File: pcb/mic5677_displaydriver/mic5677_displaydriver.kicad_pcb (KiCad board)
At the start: 2 copper layers, 180 x 110 mm, 81 parts, among them J1 Segment DIP14, J2 Segment DIP14, J3 Segment Wire Connector, J4 Common Cathode Enable, J5 PSU, J6 Bypass, J7 Serial Debug, J8 8P8C, Q1 D45H8G, Q10 BC546, Q11 BC546, Q12 BC546, Q13 BC546, Q14 BC546, Q15 BC546, Q16 BC546, Q17 BC546, Q18 BC546, Q19 BC546, Q2 D45H8G, Q20 BC546, Q21 BC546, Q22 BC546, Q23 BC546, Q3 D45H8G, Q4 D45H8G, Q5 D45H8G, Q6 D45H8G, Q7 D45H8G, Q8 D45H8G, Q9 D45H8G, U1 L7805, U2 74HC595, U3 74HC595, U4 74HC02

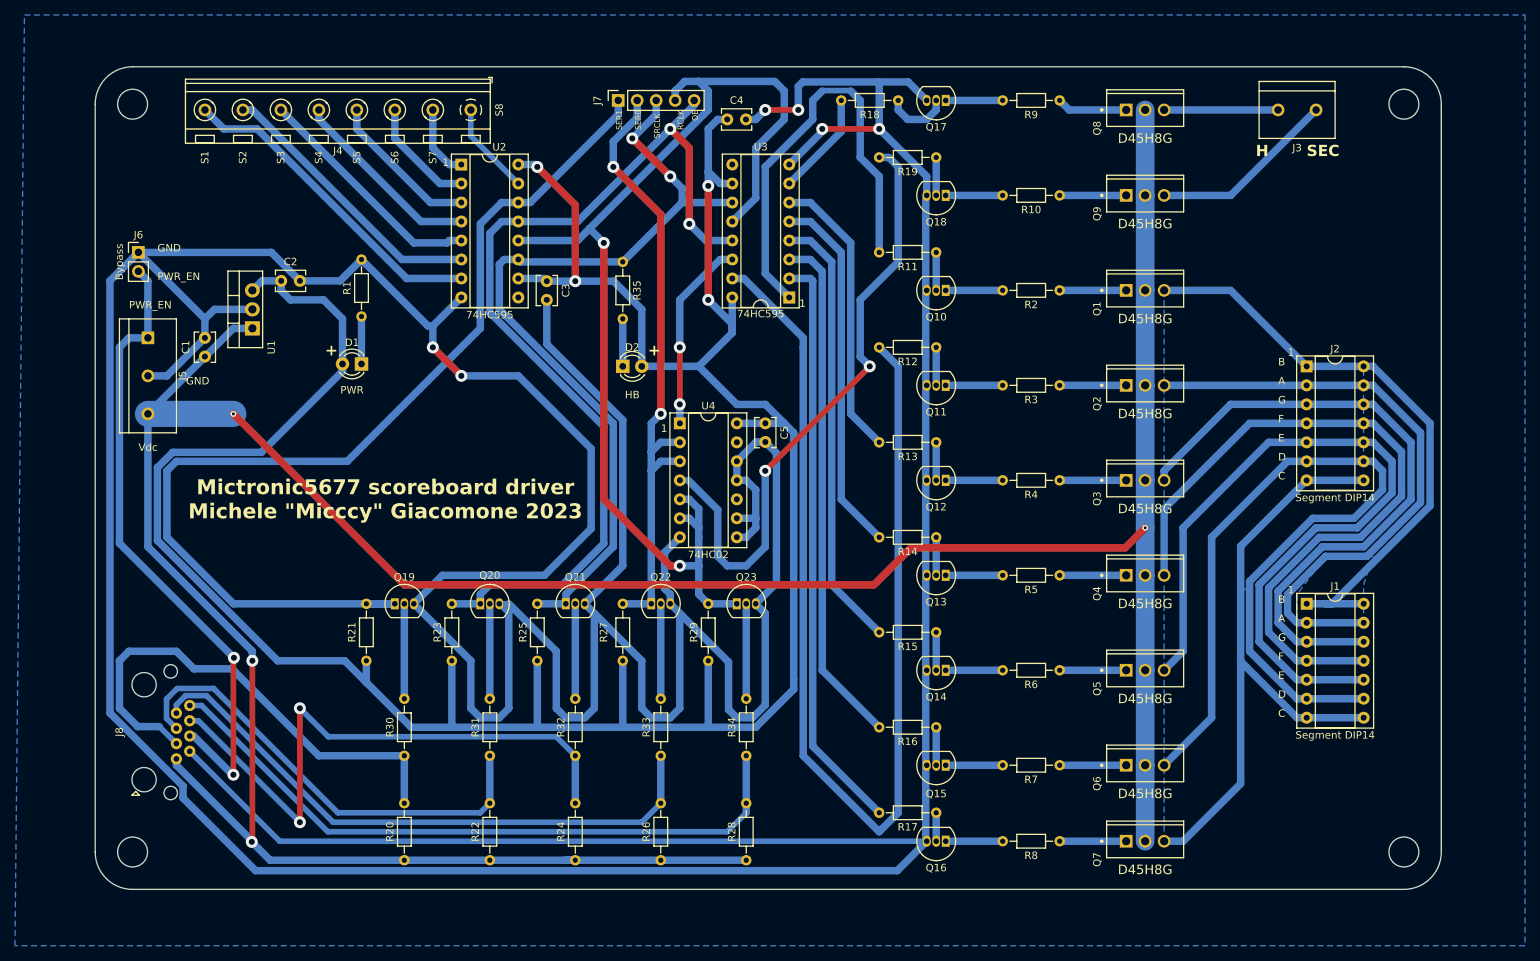
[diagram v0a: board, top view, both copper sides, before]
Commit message: Made display driver pcb work both with and without filled fill zones
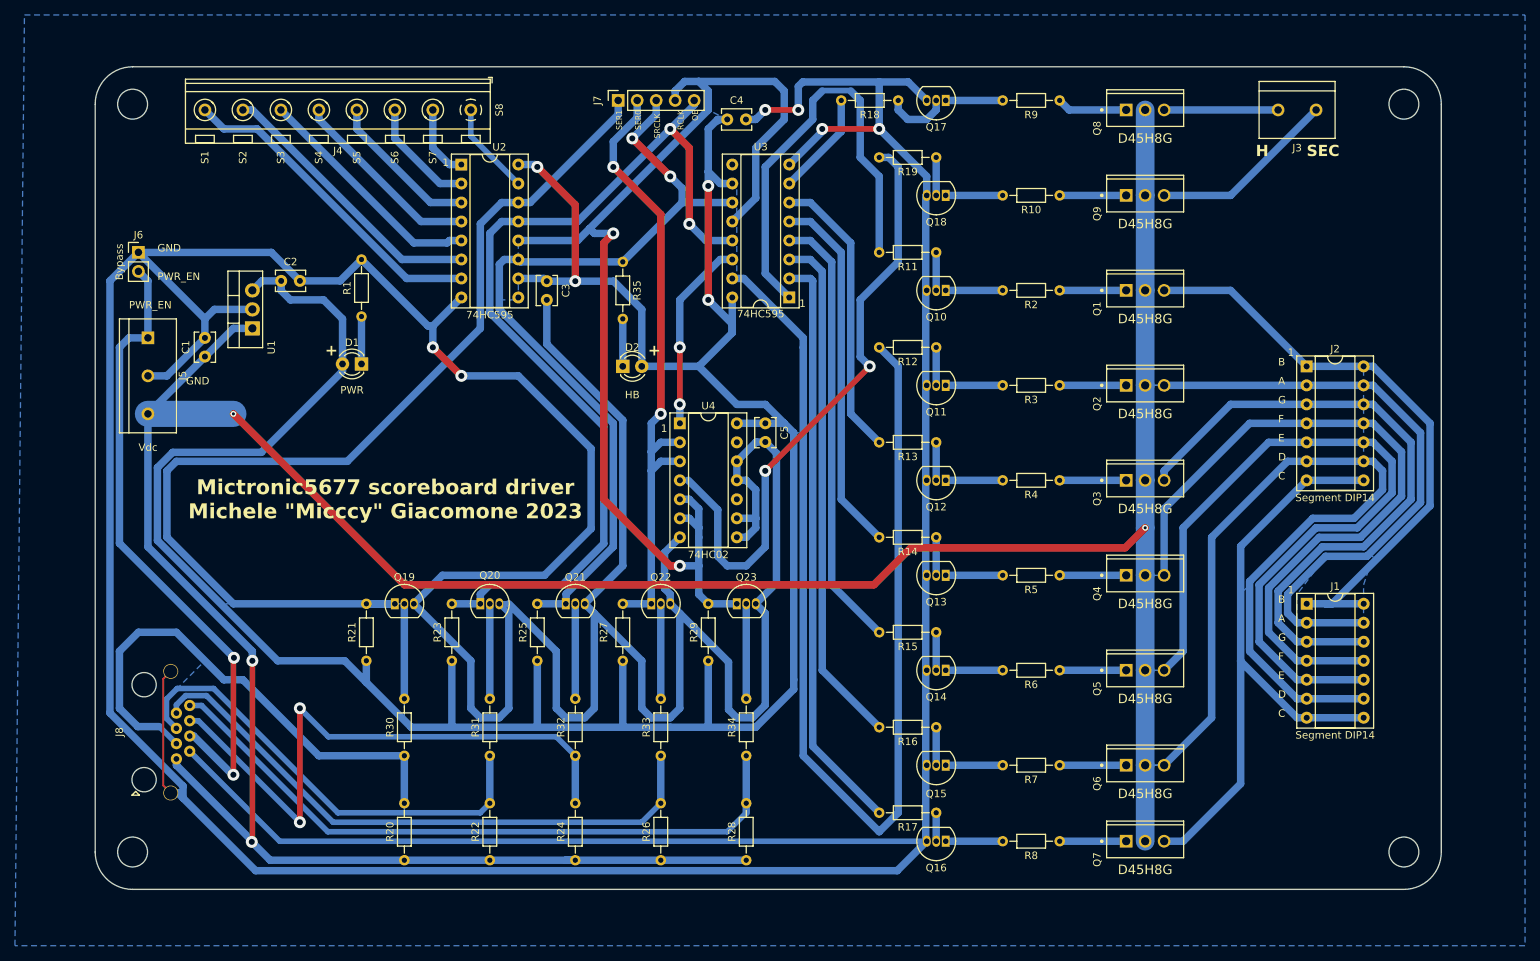
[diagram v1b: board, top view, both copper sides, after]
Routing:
- net GND: track 839.3 -> 858.3 mm
- net /SER1_IN: track 66.7 -> 69.5 mm
- net RCLK: track 150.7 -> 153.3 mm
- added copper zone on B.Cu, net +5V
- added copper zone on B.Cu, net /OE_IN
